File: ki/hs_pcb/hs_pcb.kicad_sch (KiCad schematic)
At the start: 3 parts, among them U1 74LVC163, U2 MR5A16A, X1 CXO_DIP8

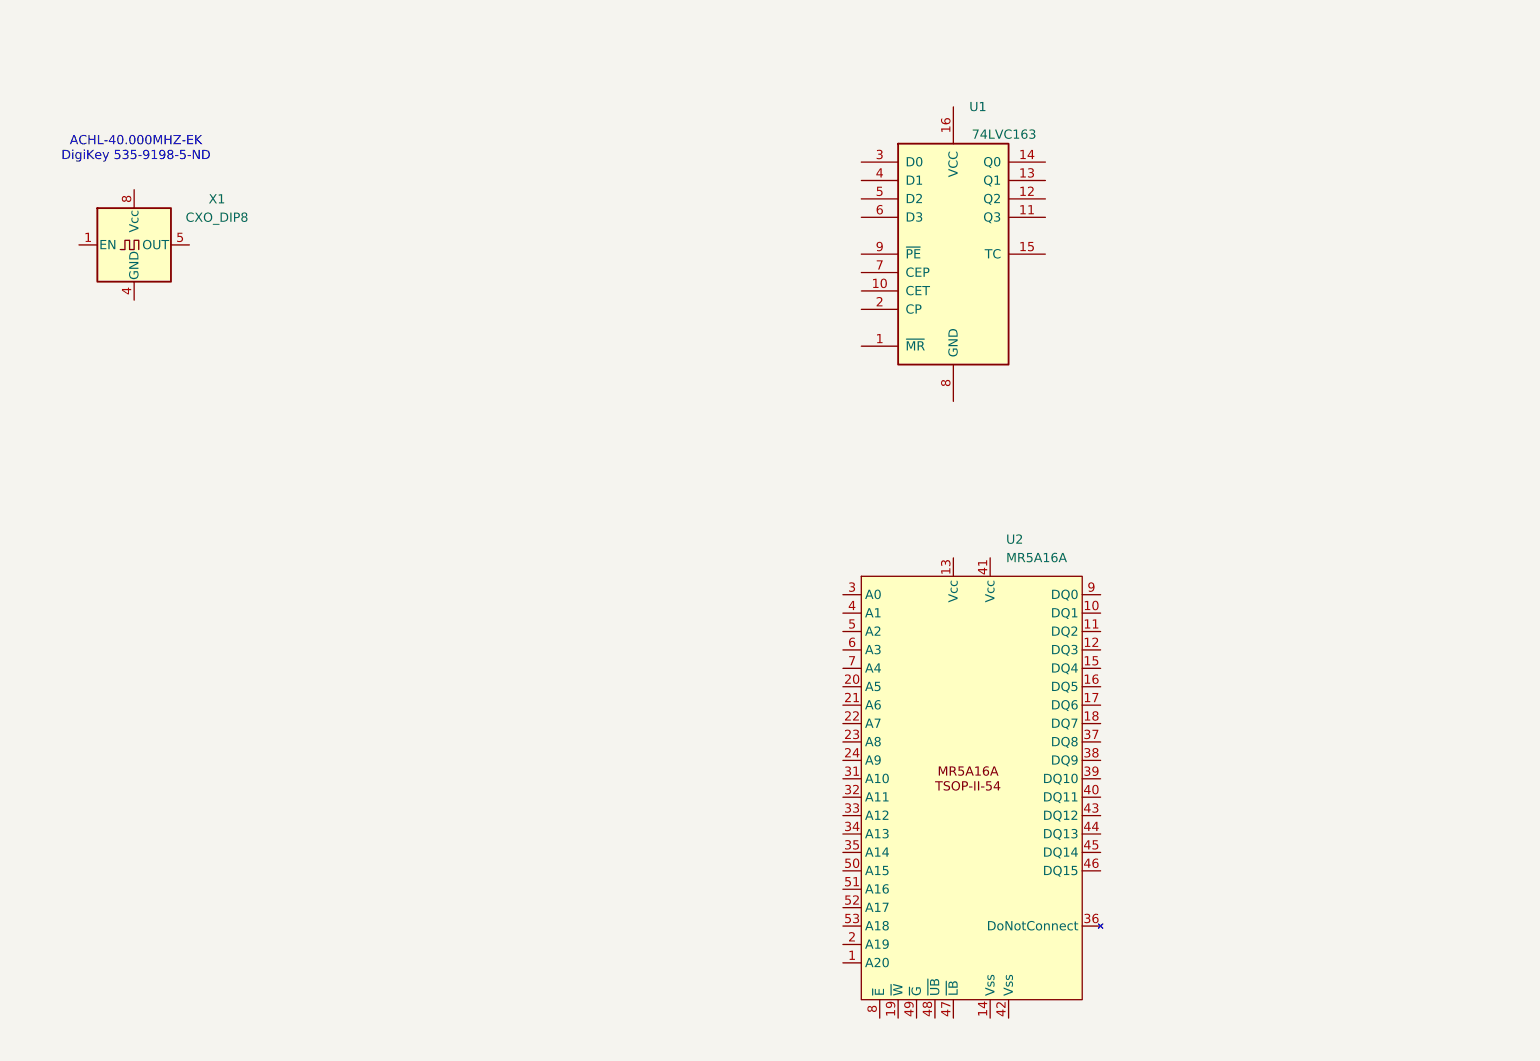
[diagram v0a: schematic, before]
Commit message: Create a 100mm square box and add some 16-bit components
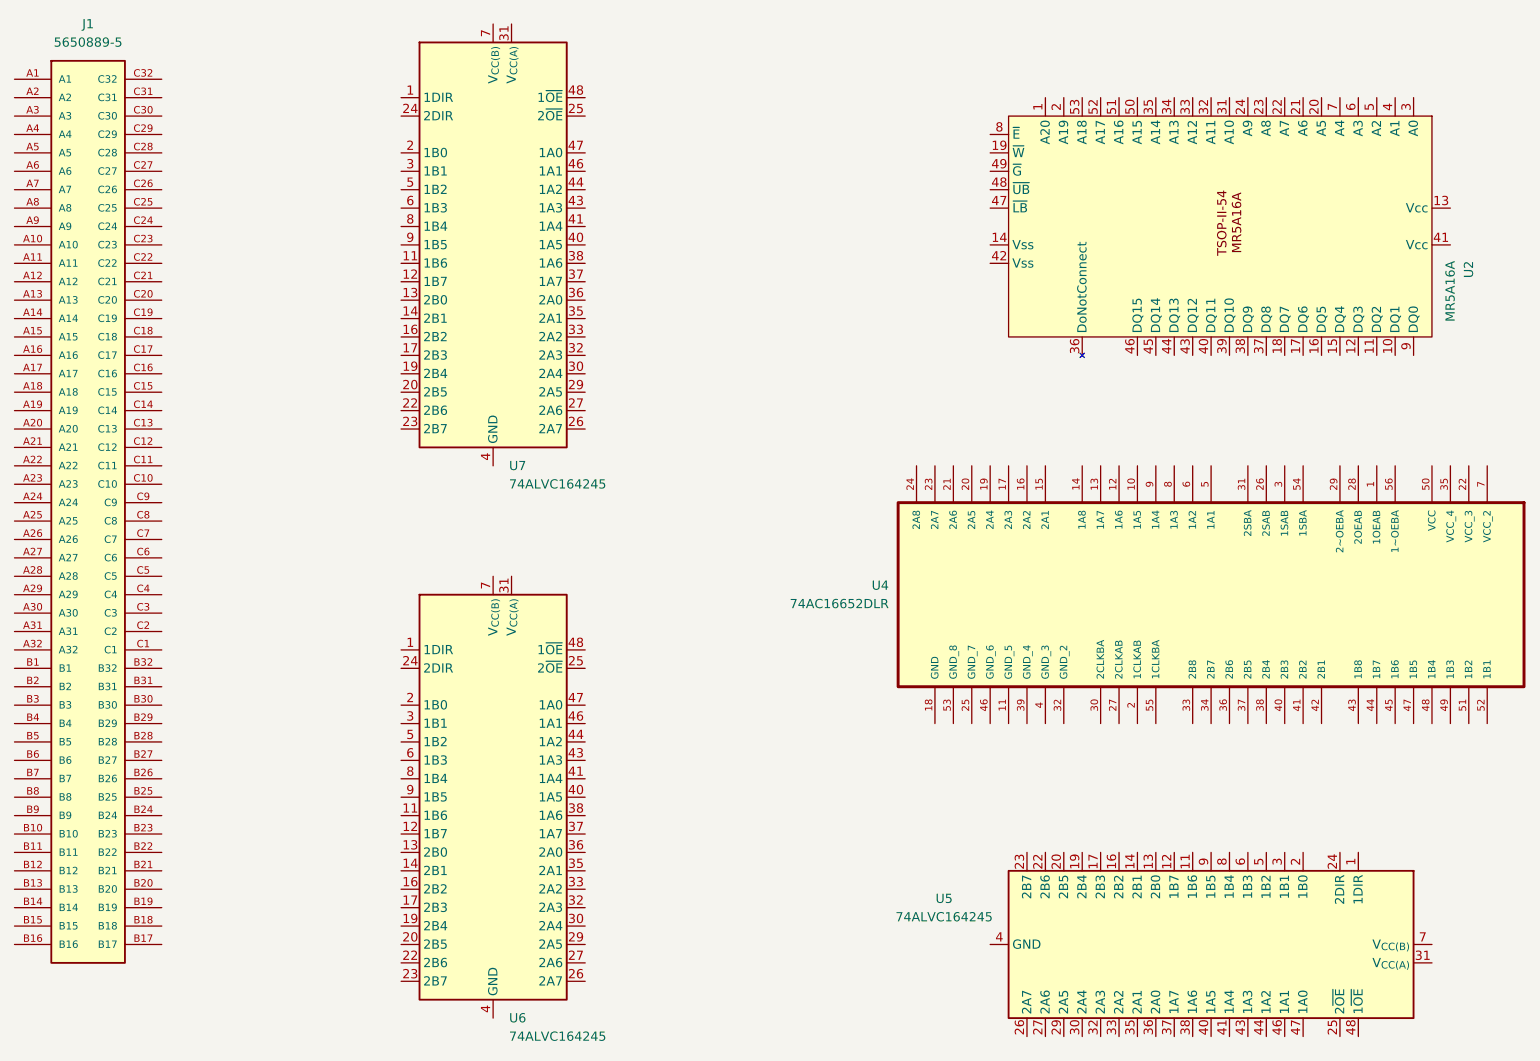
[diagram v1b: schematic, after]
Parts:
- removed U1: 74LVC163, Package_SO:TSSOP-16-1EP_4.4x5mm_P0.65mm, symbol 74xx:74LS163
- removed X1: CXO_DIP8, Oscillator:Oscillator_DIP-8, symbol Oscillator:CXO_DIP8
- added J1: 5650889-5, 5650889-5:TE_5650889-5, symbol 5650889-5:5650889-5
- added U4: 74AC16652DLR, 74AC16652DLR:SOP63P1035X279-56N, symbol 74AC16652DLR:74AC16652DLR
- added U5, U6, U7: 74ALVC164245, Package_SO:TSSOP-48_6.1x12.5mm_P0.5mm, symbol 74xx:74ALVC164245
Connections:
- new net: U7.10 (GND), U7.15 (GND), U7.21 (GND), U7.28 (GND), U7.34 (GND), U7.39 (GND), U7.4 (GND), U7.45 (GND)
- new net: U7.18 (V_{CC(B)}), U7.7 (V_{CC(B)})
- new net: U7.31 (V_{CC(A)}), U7.42 (V_{CC(A)})
- new net: U6.10 (GND), U6.15 (GND), U6.21 (GND), U6.28 (GND), U6.34 (GND), U6.39 (GND), U6.4 (GND), U6.45 (GND)
- new net: U6.18 (V_{CC(B)}), U6.7 (V_{CC(B)})
- new net: U6.31 (V_{CC(A)}), U6.42 (V_{CC(A)})
- new net: U5.10 (GND), U5.15 (GND), U5.21 (GND), U5.28 (GND), U5.34 (GND), U5.39 (GND), U5.4 (GND), U5.45 (GND)
- new net: U5.18 (V_{CC(B)}), U5.7 (V_{CC(B)})
- new net: U5.31 (V_{CC(A)}), U5.42 (V_{CC(A)})
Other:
- note removed: "ACHL-40.000MHZ-EK DigiKey 535-9198-5-ND"
- moved on the sheet: U2
